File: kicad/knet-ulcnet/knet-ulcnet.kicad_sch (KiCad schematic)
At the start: 24 parts, among them J1 Conn_01x02_Socket, J3 Conn_01x04, J4 Conn_01x02, J5 Conn_01x02_Socket, SW1 SW_SPST, U1 MC3487N, U11 Mainboard, U2 MC3486N, U3 74LS06, U4 74LS157, U5 74LS157, U6 74LS157, U9 74LS04, X11 SIO0-DIP-40, X3 74LS123

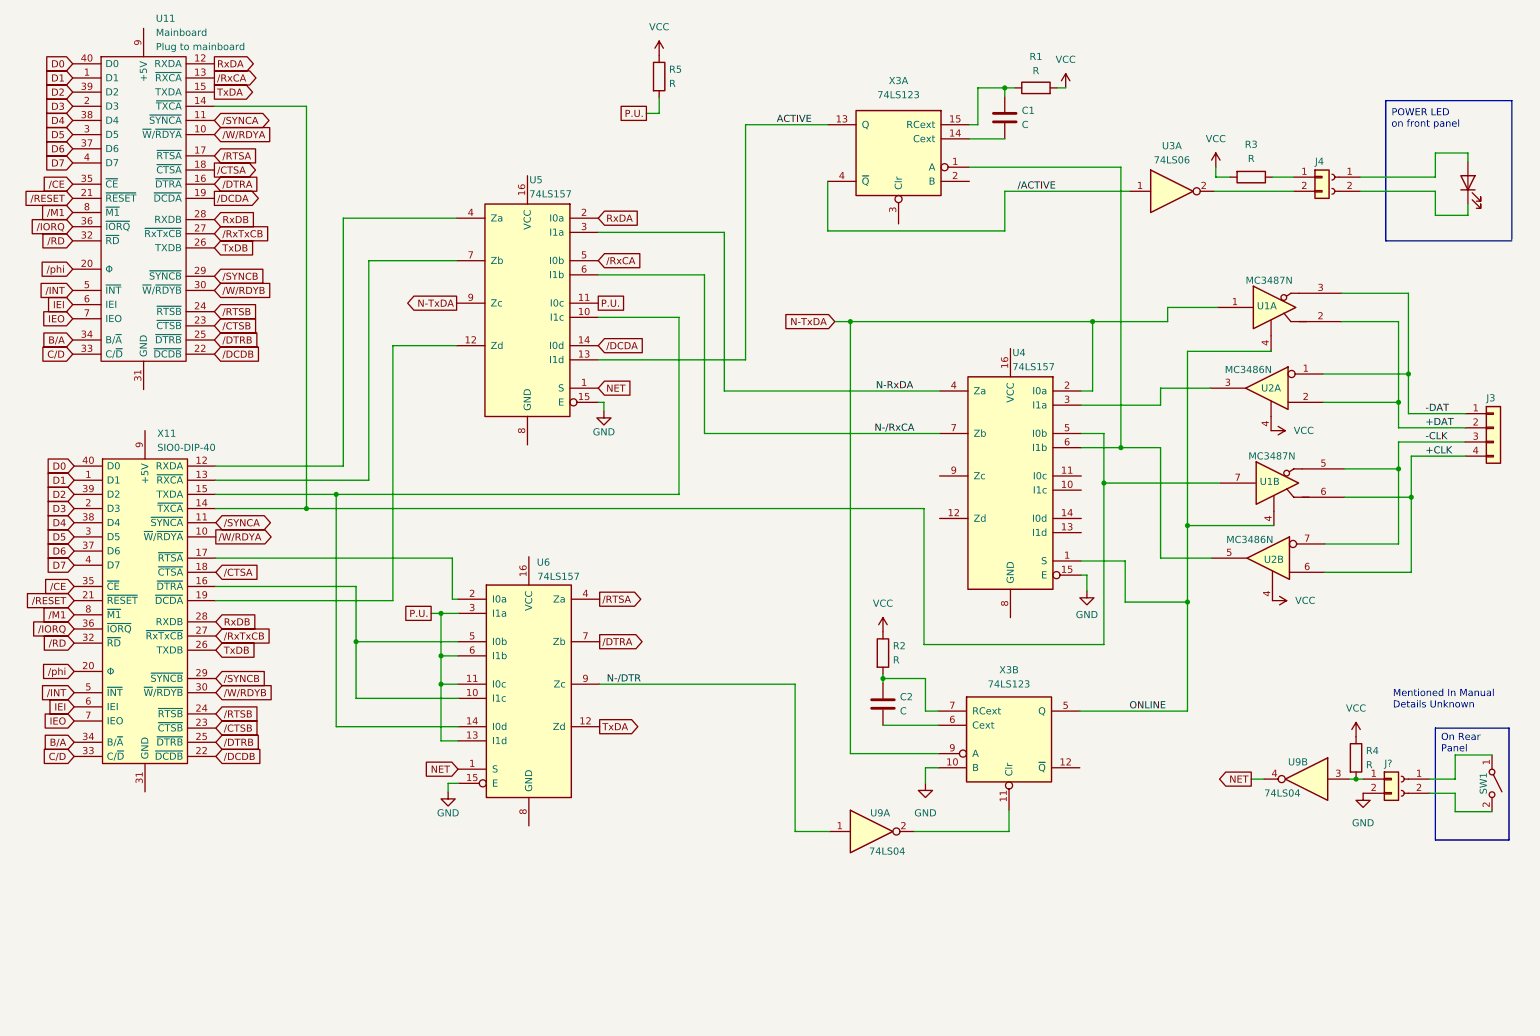
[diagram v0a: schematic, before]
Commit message: update kaynet-ulcnet schematic
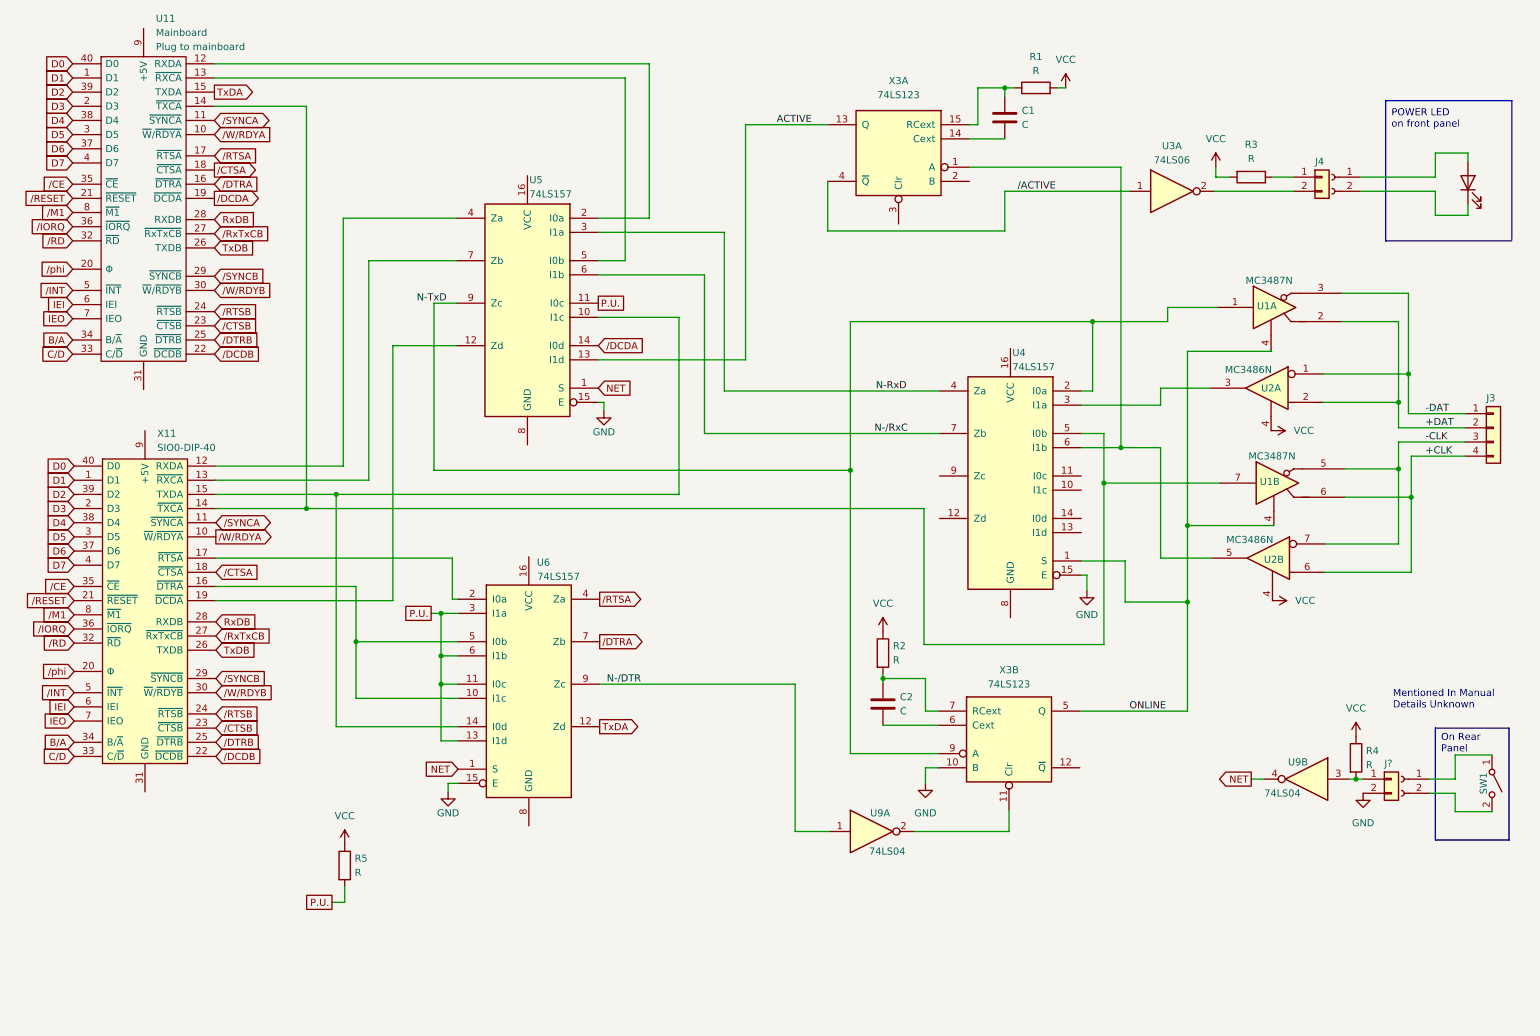
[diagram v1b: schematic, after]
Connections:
- net N-RxDA renamed N-RxD
- net N-TxDA renamed N-TxD
- net N-/RxCA renamed N-/RxC
- net RxDA: no longer names the net of U11.12 (RXDA), U5.2 (I0a)
- net /RxCA: no longer names the net of U11.13 (~{RXCA}), U5.5 (I0b)
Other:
- moved on the sheet: R5
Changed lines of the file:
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@@
   (junction (at 263.398 78.74) (diameter 0) (color 0 0 0 0)
   )
-  (junction (at 163.322 69.342) (diameter 0) (color 0 0 0 0)
-  )
   (junction (at 261.62 95.758) (diameter 0) (color 0 0 0 0)
   )
@@
   (junction (at 208.788 98.298) (diameter 0) (color 0 0 0 0)
   )
+  (junction (at 163.322 96.012) (diameter 0) (color 0 0 0 0)
+  )
   (junction (at 223.774 105.918) (diameter 0) (color 0 0 0 0)
   )
@@
     (stroke (width 0) (type default))
   )
+  (wire (pts (xy 88.646 66.04) (xy 88.646 96.012))
+    (stroke (width 0) (type default))
+  )
   (wire (pts (xy 211.836 41.656) (xy 211.836 91.948))
     (stroke (width 0) (type default))
@@
     (stroke (width 0) (type default))
   )
+  (wire (pts (xy 127.254 23.114) (xy 127.254 50.8))
+    (stroke (width 0) (type default))
+  )
   (polyline (pts (xy 281.432 162.306) (xy 268.224 162.306))
     (stroke (width 0) (type default))
@@
     (stroke (width 0) (type default))
   )
+  (wire (pts (xy 127.254 50.8) (xy 118.11 50.8))
+    (stroke (width 0) (type default))
+  )
   (wire (pts (xy 92.964 121.666) (xy 89.916 121.666))
     (stroke (width 0) (type default))
@@
     (stroke (width 0) (type default))
   )
+  (wire (pts (xy 92.71 66.04) (xy 88.646 66.04))
+    (stroke (width 0) (type default))
+  )
   (wire (pts (xy 89.916 129.286) (xy 89.916 121.666))
     (stroke (width 0) (type default))
@@
     (stroke (width 0) (type default))
   )
+  (wire (pts (xy 49.276 25.654) (xy 122.936 25.654))
+    (stroke (width 0) (type default))
+  )
   (wire (pts (xy 235.204 151.384) (xy 237.49 151.384))
     (stroke (width 0) (type default))
@@
     (stroke (width 0) (type default))
   )
+  (wire (pts (xy 49.276 23.114) (xy 127.254 23.114))
+    (stroke (width 0) (type default))
+  )
   (wire (pts (xy 268.224 50.292) (xy 274.066 50.292))
     (stroke (width 0) (type default))
@@
     (stroke (width 0) (type default))
   )
-  (wire (pts (xy 163.322 69.342) (xy 163.322 146.812))
+  (wire (pts (xy 163.322 69.342) (xy 163.322 96.012))
     (stroke (width 0) (type default))
   )
@@
     (stroke (width 0) (type default))
   )
+  (wire (pts (xy 88.646 96.012) (xy 163.322 96.012))
+    (stroke (width 0) (type default))
+  )
   (wire (pts (xy 92.964 136.906) (xy 74.676 136.906))
     (stroke (width 0) (type default))
@@
     (stroke (width 0) (type default))
   )
+  (wire (pts (xy 122.936 25.654) (xy 122.936 58.42))
+    (stroke (width 0) (type default))
+  )
   (polyline (pts (xy 259.334 29.718) (xy 259.334 54.864))
     (stroke (width 0) (type default))
   )
+  (wire (pts (xy 163.322 96.012) (xy 163.322 146.812))
+    (stroke (width 0) (type default))
+  )
   (wire (pts (xy 76.962 58.42) (xy 92.71 58.42))
     (stroke (width 0) (type default))
@@
     (stroke (width 0) (type default))
   )
-  (wire (pts (xy 129.032 29.21) (xy 129.032 32.004))
+  (wire (pts (xy 72.644 170.688) (xy 72.644 173.482))
     (stroke (width 0) (type default))
   )
@@
     (stroke (width 0) (type default))
   )
-  (wire (pts (xy 160.528 69.342) (xy 163.322 69.342))
-    (stroke (width 0) (type default))
-  )
   (wire (pts (xy 274.066 50.292) (xy 274.066 48.26))
     (stroke (width 0) (type default))
@@
     (stroke (width 0) (type default))
   )
-  (wire (pts (xy 129.032 32.004) (xy 126.746 32.004))
+  (wire (pts (xy 72.644 173.482) (xy 70.358 173.482))
     (stroke (width 0) (type default))
   )
@@
     (stroke (width 0) (type default))
   )
+  (wire (pts (xy 122.936 58.42) (xy 118.11 58.42))
+    (stroke (width 0) (type default))
+  )
   (wire (pts (xy 144.526 34.036) (xy 159.258 34.036))
     (stroke (width 0) (type default))
@@
     (effects (font (size 1.27 1.27)) (justify left bottom))
   )
+  (label "N-TxD" (at 90.932 66.04 180) (fields_autoplaced)
+    (effects (font (size 1.27 1.27)) (justify right bottom))
+  )
   (label "+DAT" (at 266.446 88.392 0) (fields_autoplaced)
     (effects (font (size 1.27 1.27)) (justify left bottom))
@@
     (effects (font (size 1.27 1.27)) (justify left bottom))
   )
-  (label "N-{slash}RxCA" (at 167.64 89.408 0) (fields_autoplaced)
+  (label "N-{slash}RxC" (at 167.64 89.408 0) (fields_autoplaced)
     (effects (font (size 1.27 1.27)) (justify left bottom))
   )
@@
     (effects (font (size 1.27 1.27)) (justify left bottom))
   )
-  (label "N-RxDA" (at 167.894 81.788 0) (fields_autoplaced)
+  (label "N-RxD" (at 167.894 81.788 0) (fields_autoplaced)
     (effects (font (size 1.27 1.27)) (justify left bottom))
   )
@@
     )
   )
-  (global_label "P.U." (shape passive) (at 126.746 32.004 180) (fields_autoplaced)
-    (effects (font (size 1.27 1.27)) (justify right))
-    (property "Intersheetrefs" "${INTERSHEET_REFS}" (at 121.062 32.004 0)
+  (global_label "P.U." (shape passive) (at 70.358 173.482 180) (fields_autoplaced)
+    (effects (font (size 1.27 1.27)) (justify right))
+    (property "Intersheetrefs" "${INTERSHEET_REFS}" (at 64.674 173.482 0)
       (effects (font (size 1.27 1.27)) (justify right) hide)
     )
@@
     )
   )
-  (global_label "RxDA" (shape output) (at 49.276 23.114 0) (fields_autoplaced)
-    (effects (font (size 1.27 1.27)) (justify left))
-    (property "Intersheetrefs" "${INTERSHEET_REFS}" (at 56.9179 23.114 0)
-      (effects (font (size 1.27 1.27)) (justify left) hide)
-    )
-  )
   (global_label "TxDB" (shape input) (at 49.276 56.134 0) (fields_autoplaced)
     (effects (font (size 1.27 1.27)) (justify left))
@@
     )
   )
-  (global_label "{slash}RxCA" (shape input) (at 118.11 58.42 0) (fields_autoplaced)
-    (effects (font (size 1.27 1.27)) (justify left))
-    (property "Intersheetrefs" "${INTERSHEET_REFS}" (at 127.0824 58.42 0)
-      (effects (font (size 1.27 1.27)) (justify left) hide)
-    )
-  )
   (global_label "RxDB" (shape input) (at 49.53 123.19 0) (fields_autoplaced)
     (effects (font (size 1.27 1.27)) (justify left))
@@
     )
   )
-  (global_label "N-TxDA" (shape input) (at 160.528 69.342 180) (fields_autoplaced)
-    (effects (font (size 1.27 1.27)) (justify right))
-    (property "Intersheetrefs" "${INTERSHEET_REFS}" (at 150.2856 69.342 0)
-      (effects (font (size 1.27 1.27)) (justify right) hide)
-    )
-  )
-  (global_label "RxDA" (shape input) (at 118.11 50.8 0) (fields_autoplaced)
-    (effects (font (size 1.27 1.27)) (justify left))
-    (property "Intersheetrefs" "${INTERSHEET_REFS}" (at 125.7519 50.8 0)
-      (effects (font (size 1.27 1.27)) (justify left) hide)
-    )
-  )
   (global_label "NET" (shape input) (at 92.964 149.606 180) (fields_autoplaced)
     (effects (font (size 1.27 1.27)) (justify right))
@@
     )
   )
-  (global_label "N-TxDA" (shape output) (at 92.71 66.04 180) (fields_autoplaced)
-    (effects (font (size 1.27 1.27)) (justify right))
-    (property "Intersheetrefs" "${INTERSHEET_REFS}" (at 82.4676 66.04 0)
-      (effects (font (size 1.27 1.27)) (justify right) hide)
-    )
-  )
   (global_label "{slash}CE" (shape input) (at 24.13 116.84 180) (fields_autoplaced)
     (effects (font (size 1.27 1.27)) (justify right))
@@
     (property "Intersheetrefs" "${INTERSHEET_REFS}" (at 17.1534 121.92 0)
       (effects (font (size 1.27 1.27)) (justify right) hide)
-    )
-  )
-  (global_label "{slash}RxCA" (shape output) (at 49.276 25.654 0) (fields_autoplaced)
-    (effects (font (size 1.27 1.27)) (justify left))
-    (property "Intersheetrefs" "${INTERSHEET_REFS}" (at 58.2484 25.654 0)
-      (effects (font (size 1.27 1.27)) (justify left) hide)
     )
   )
@@
     )
   )
-  (symbol (lib_id "power:VCC") (at 129.032 21.59 0) (unit 1)
+  (symbol (lib_id "power:VCC") (at 72.644 163.068 0) (unit 1)
     (in_bom yes) (on_board yes) (dnp no) (fields_autoplaced)
-    (property "Reference" "#PWR012" (at 129.032 25.4 0)
+    (property "Reference" "#PWR012" (at 72.644 166.878 0)
       (effects (font (size 1.27 1.27)) hide)
     )
-    (property "Value" "VCC" (at 129.032 16.51 0)
+    (property "Value" "VCC" (at 72.644 157.988 0)
       (effects (font (size 1.27 1.27)))
     )
-    (property "Footprint" "" (at 129.032 21.59 0)
+    (property "Footprint" "" (at 72.644 163.068 0)
       (effects (font (size 1.27 1.27)) hide)
     )
-    (property "Datasheet" "" (at 129.032 21.59 0)
+    (property "Datasheet" "" (at 72.644 163.068 0)
       (effects (font (size 1.27 1.27)) hide)
     )
@@
     )
   )
-  (symbol (lib_id "Device:R") (at 129.032 25.4 0) (unit 1)
+  (symbol (lib_id "Device:R") (at 72.644 166.878 0) (unit 1)
     (in_bom yes) (on_board yes) (dnp no) (fields_autoplaced)
-    (property "Reference" "R5" (at 130.81 24.13 0)
+    (property "Reference" "R5" (at 74.422 165.608 0)
       (effects (font (size 1.27 1.27)) (justify left))
     )
-    (property "Value" "R" (at 130.81 26.67 0)
+    (property "Value" "R" (at 74.422 168.148 0)
       (effects (font (size 1.27 1.27)) (justify left))
     )
-    (property "Footprint" "" (at 127.254 25.4 90)
+    (property "Footprint" "" (at 70.866 166.878 90)
       (effects (font (size 1.27 1.27)) hide)
     )
-    (property "Datasheet" "~" (at 129.032 25.4 0)
+    (property "Datasheet" "~" (at 72.644 166.878 0)
       (effects (font (size 1.27 1.27)) hide)
     )

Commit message: refinement of KayNet ULCNET schematic
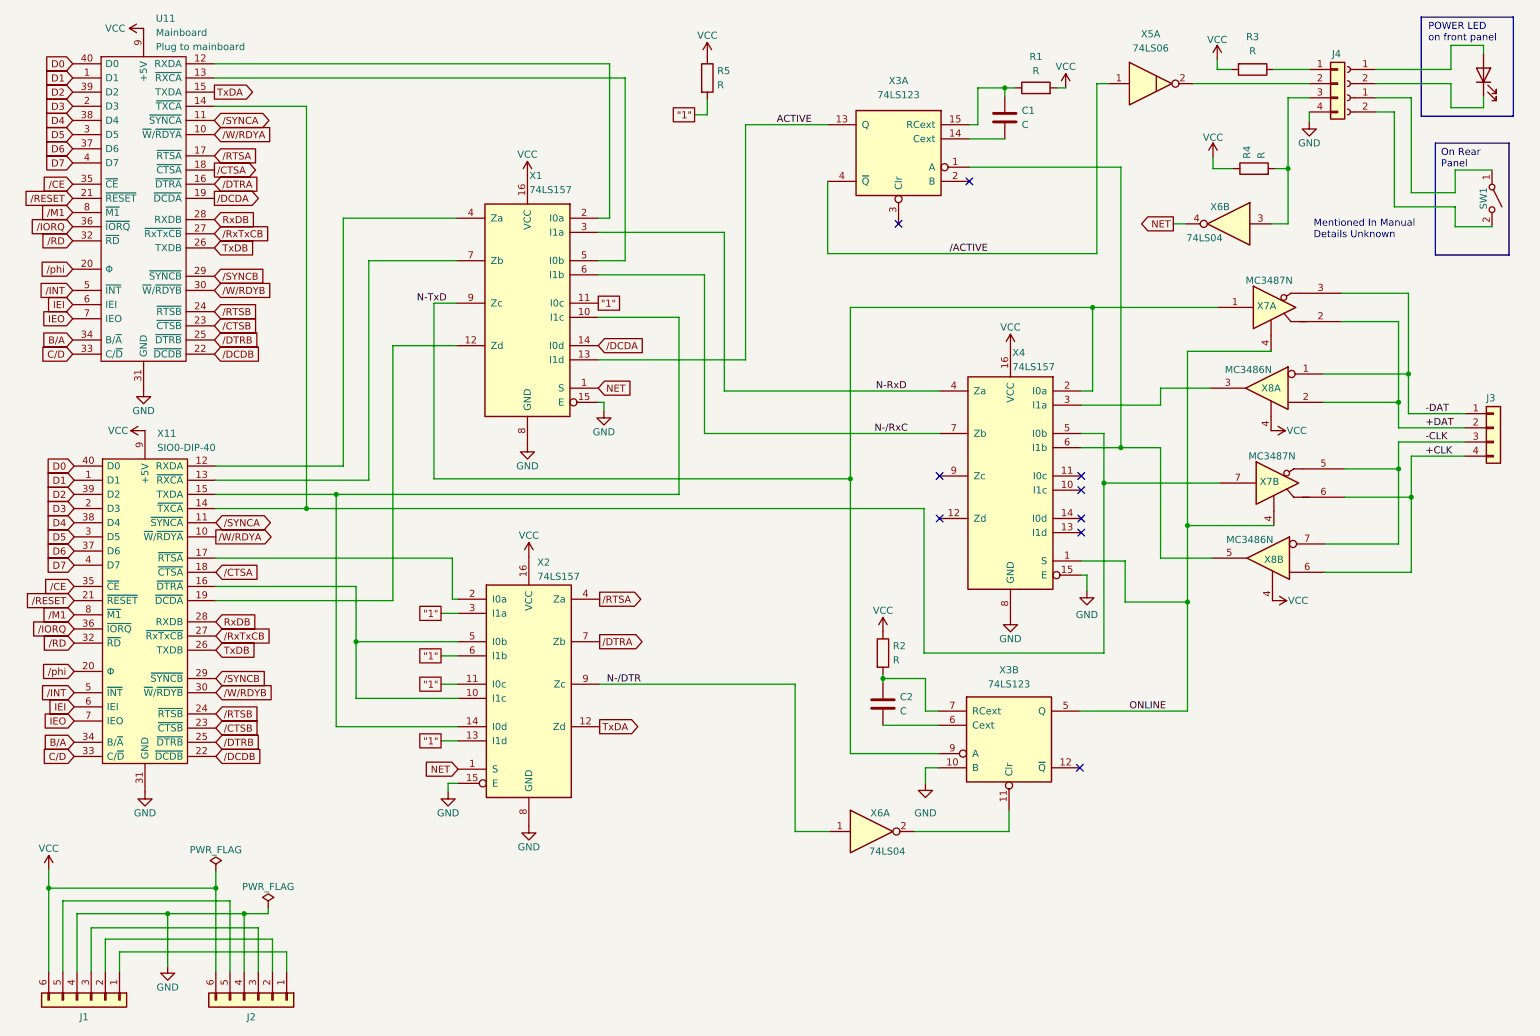
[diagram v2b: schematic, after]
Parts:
- removed J4, J?: Conn_01x02, symbol Connector_Generic:Conn_01x02
- added J1, J2: Conn_01x06, symbol Connector_Generic:Conn_01x06
- added J4: Conn_01x04, symbol Connector_Generic:Conn_01x04
- renumbered U5 to X1, U6 to X2, U4 to X4, U3 to X5, U9 to X6, U1 to X7, U2 to X8
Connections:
- net GND: now also U11.31 (GND), X1.8 (GND), X11.31 (GND), X2.8 (GND), X4.8 (GND), J1.4 (Pin_4), J2.4 (Pin_4), J4.4 (Pin_4)
- net VCC: now also U11.9 (+5V), X1.16 (VCC), X11.9 (+5V), X2.16 (VCC), X4.16 (VCC), J1.6 (Pin_6), J2.6 (Pin_6)
- net at R4.2, X6.3: now also J4.3 (Pin_3)
- net at R3.1: now also J4.1 (Pin_1)
- net at X5.2: now also J4.2 (Pin_2)
- net P.U. renamed "1"
- new net: J1.1 (Pin_1), J2.1 (Pin_1)
- new net: J1.2 (Pin_2), J2.2 (Pin_2)
- new net: J1.3 (Pin_3), J2.3 (Pin_3)
- new net: J1.5 (Pin_5), J2.5 (Pin_5)
- no-connect marks 0 -> 9
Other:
- moved on the sheet: R3, R4, R5, SW1, X6B
